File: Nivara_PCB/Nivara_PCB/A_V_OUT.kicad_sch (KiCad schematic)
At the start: 8 parts, among them U10 GP8201S-TC50-EW

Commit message: TERMINACIONES Y AJUSTES FINALES
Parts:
- removed R26: 10K, PCM_Resistor_SMD_AKL:R_0603_1608Metric, symbol EasyEDA:R_0603
- added R30: 10k, PCM_Resistor_SMD_AKL:R_0603_1608Metric, symbol EasyEDA:R_0603
- C11: value 0.1uF -> 100nF; LCSC Part (none) -> C77058; Part # (none) -> GRM188R72A104KA35D; Vol 15V -> (none)
- C12: LCSC Part (none) -> C15849; Part # (none) -> CL10A105KB8NNNC; Vol 15V -> (none)
- D19: LCSC Part (none) -> C134947; Part # (none) -> SMAJ12A-13-F
- R27: renamed from R23; LCSC Part (none) -> C99782; Part # (none) -> RC0603FR-074K7L
- R28: renamed from R24; LCSC Part (none) -> C99782; Part # (none) -> RC0603FR-074K7L
- R29: renamed from R25; LCSC Part (none) -> C21189; Part # (none) -> 0603WAF0000T5E
- U12: renamed from U10; Part # (none) -> GP8201S-TC50-EW
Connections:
- net +3.3V: now also R30.1
- net ESP_SEL_VOUT: now also R30.2

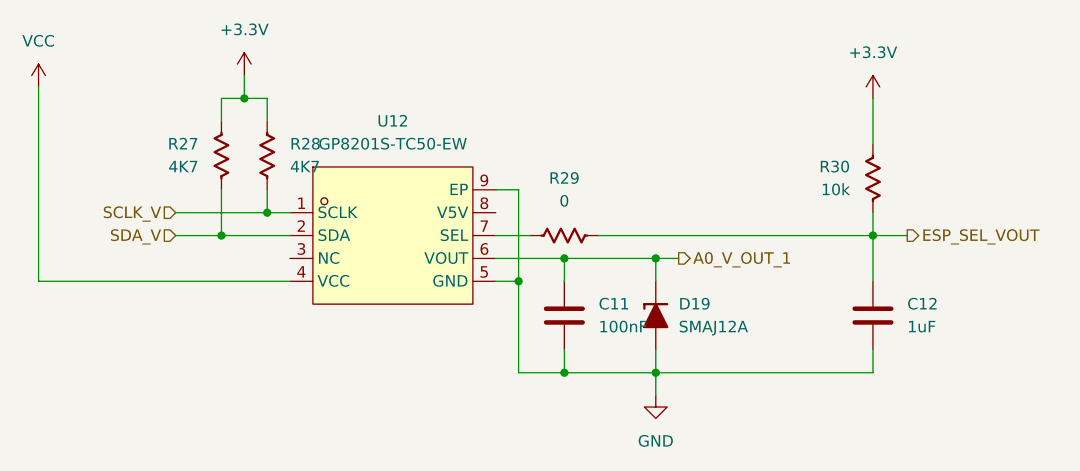
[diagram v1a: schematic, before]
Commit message: Cambios en las silscreen de los componentes.
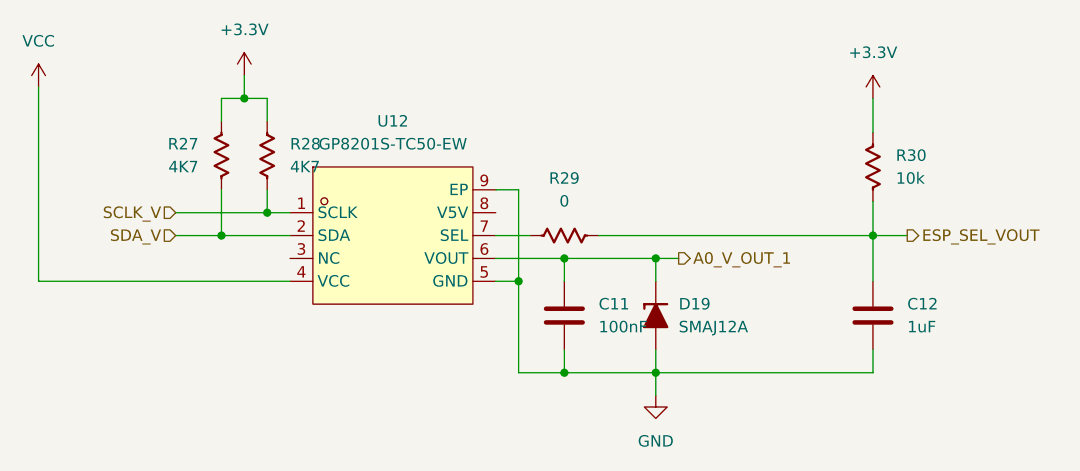
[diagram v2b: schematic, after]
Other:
- moved on the sheet: R30
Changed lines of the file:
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@@
 	(wire
 		(pts
-			(xy 152.4 64.77) (xy 152.4 67.31)
+			(xy 152.4 63.5) (xy 152.4 67.31)
 		)
 		(stroke
@@
 	(wire
 		(pts
-			(xy 152.4 52.07) (xy 152.4 57.15)
+			(xy 152.4 52.07) (xy 152.4 55.88)
 		)
 		(stroke
@@
 		(dnp no)
 		(fields_autoplaced yes)
-		(property "Reference" "#PWR047"
+		(property "Reference" "#PWR049"
 			(at 128.27 91.44 0)
 			(effects
@@
 			(project "Nivara_PCB"
 				(path "/13184db0-a71d-4054-b13a-bbf46d2b100d/4e7fa7f2-8bf5-4f9c-874d-fa1b4fd76f92/941ecd47-882f-406e-b54e-d369029f60e5"
-					(reference "#PWR047")
+					(reference "#PWR049")
 					(unit 1)
 				)
@@
 		(dnp no)
 		(fields_autoplaced yes)
-		(property "Reference" "#PWR046"
+		(property "Reference" "#PWR048"
 			(at 82.55 53.34 0)
 			(effects
@@
 			(project "Nivara_PCB"
 				(path "/13184db0-a71d-4054-b13a-bbf46d2b100d/4e7fa7f2-8bf5-4f9c-874d-fa1b4fd76f92/941ecd47-882f-406e-b54e-d369029f60e5"
-					(reference "#PWR046")
+					(reference "#PWR048")
 					(unit 1)
 				)
@@
 		(dnp no)
 		(fields_autoplaced yes)
-		(property "Reference" "#PWR045"
+		(property "Reference" "#PWR047"
 			(at 59.69 54.61 0)
 			(effects
@@
 			(project "Nivara_PCB"
 				(path "/13184db0-a71d-4054-b13a-bbf46d2b100d/4e7fa7f2-8bf5-4f9c-874d-fa1b4fd76f92/941ecd47-882f-406e-b54e-d369029f60e5"
-					(reference "#PWR045")
+					(reference "#PWR047")
 					(unit 1)
 				)
@@
 	(symbol
 		(lib_id "EasyEDA:R_0603")
-		(at 152.4 60.96 0)
+		(at 152.4 59.69 0)
 		(mirror y)
 		(unit 1)
@@
 		(fields_autoplaced yes)
 		(property "Reference" "R30"
-			(at 149.86 59.6899 0)
-			(effects
-				(font
-					(size 1.27 1.27)
-				)
-				(justify left)
+			(at 154.94 58.4199 0)
+			(effects
+				(font
+					(size 1.27 1.27)
+				)
+				(justify right)
 			)
 		)
 		(property "Value" "10k"
-			(at 149.86 62.2299 0)
-			(effects
-				(font
-					(size 1.27 1.27)
-				)
-				(justify left)
+			(at 154.94 60.9599 0)
+			(effects
+				(font
+					(size 1.27 1.27)
+				)
+				(justify right)
 			)
 		)
 		(property "Footprint" "PCM_Resistor_SMD_AKL:R_0603_1608Metric"
-			(at 152.4 72.39 0)
+			(at 152.4 71.12 0)
 			(effects
 				(font
@@
 		)
 		(property "Datasheet" "https://jlcpcb.com/api/file/downloadByFileSystemAccessId/8579706381320323072"
-			(at 152.4 60.96 0)
+			(at 152.4 59.69 0)
 			(effects
 				(font
@@
 		)
 		(property "Description" "SMD 0603 Chip Resistor, US Symbol, Alternate KiCad Library"
-			(at 152.4 60.96 0)
+			(at 152.4 59.69 0)
 			(effects
 				(font
@@
 		)
 		(property "Part #" "0603WAF1002T5E"
-			(at 152.4 60.96 0)
+			(at 152.4 59.69 0)
 			(effects
 				(font
@@
 		)
 		(property "LCSC Part" "C25804"
-			(at 152.4 60.96 0)
+			(at 152.4 59.69 0)
 			(effects
 				(font
@@
 		(dnp no)
 		(fields_autoplaced yes)
-		(property "Reference" "#PWR048"
+		(property "Reference" "#PWR050"
 			(at 152.4 55.88 0)
 			(effects
@@
 			(project "Nivara_PCB"
 				(path "/13184db0-a71d-4054-b13a-bbf46d2b100d/4e7fa7f2-8bf5-4f9c-874d-fa1b4fd76f92/941ecd47-882f-406e-b54e-d369029f60e5"
-					(reference "#PWR048")
+					(reference "#PWR050")
 					(unit 1)
 				)
